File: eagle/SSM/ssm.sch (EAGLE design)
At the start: 21 parts, among them IC1 4051N, IC2 MCP604P

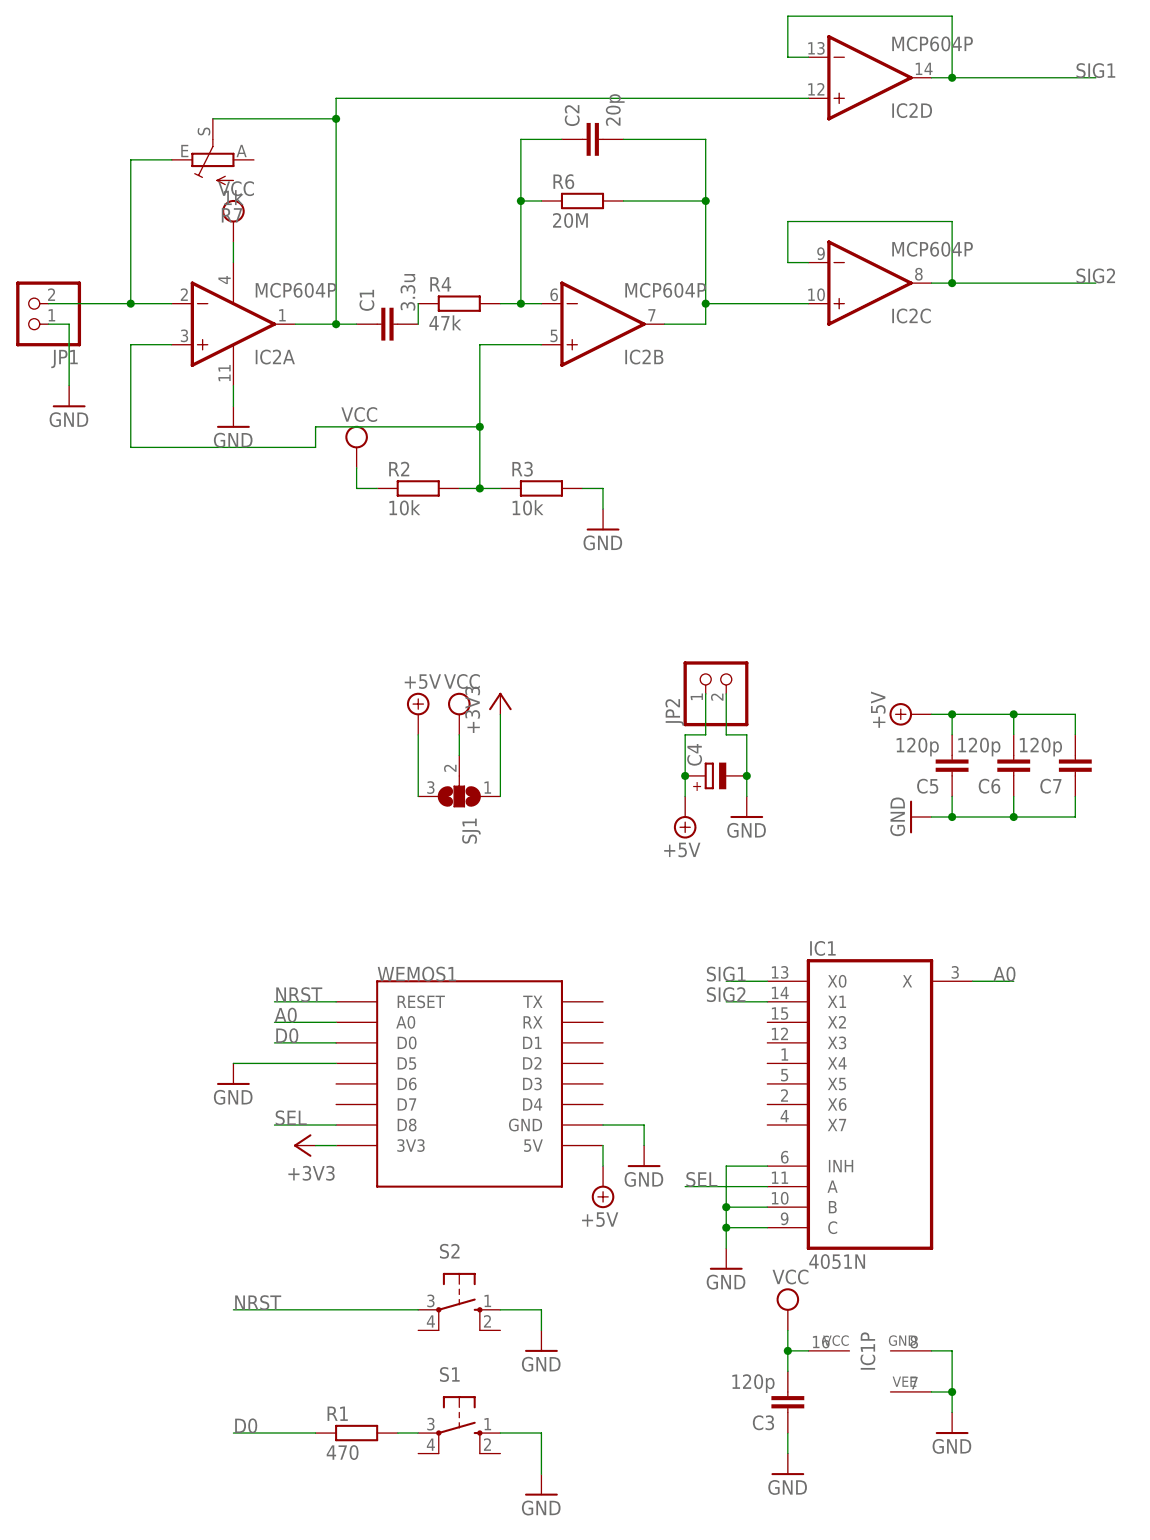
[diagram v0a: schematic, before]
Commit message: realign board for ordered parts
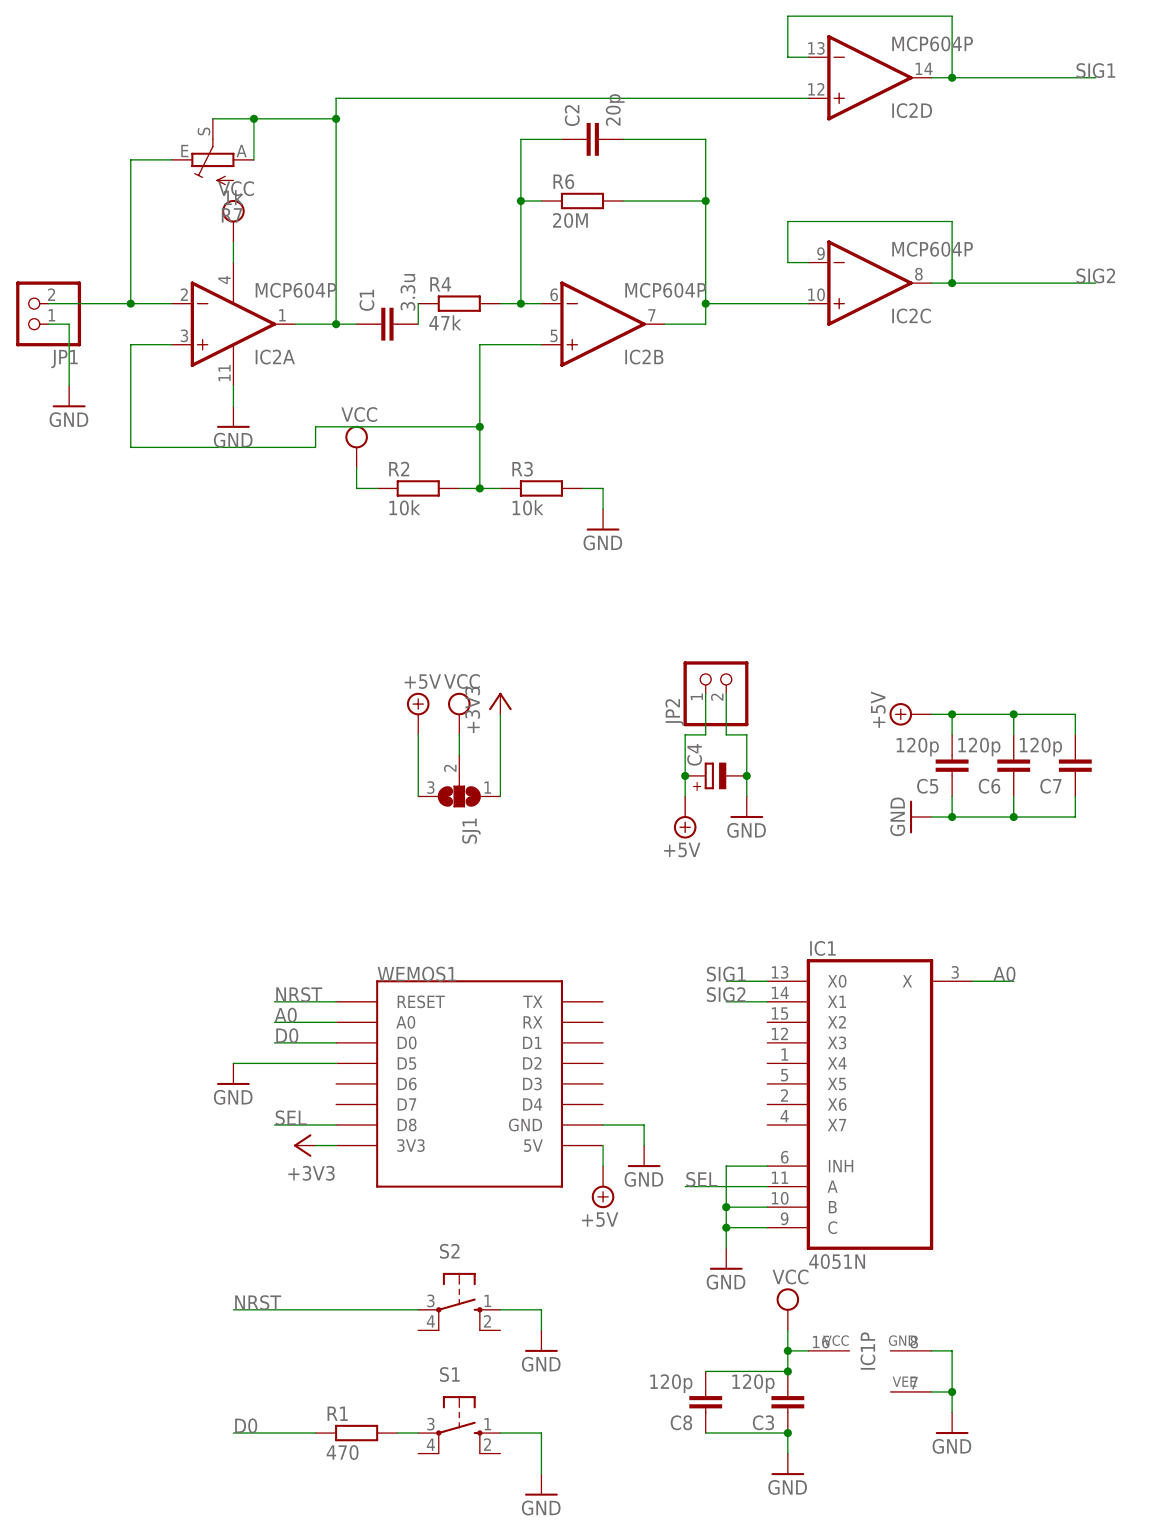
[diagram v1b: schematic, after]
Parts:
- added C8: 120p, rcl:C-EU025-024X044
- C1: device capacitor-wima:C5/3 -> Cap:C-EU
- C2, C3, C5, C6, C7: device capacitor-wima:C5/3 -> rcl:C-EU025-024X044
- R6: device resistor:R-EU_0204/7 -> rcl:R-EU_0207/10
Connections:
- net GND: now also C8.1
- net N$5: now also R7.A
- net VCC: now also C8.2
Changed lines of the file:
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@@
 <part name="GND4" library="supply1" library_urn="urn:adsk.eagle:library:371" deviceset="GND" device=""/>
 <part name="IC2" library="linear" deviceset="MCP604" device="P" value="MCP604P"/>
-<part name="P+1" library="supply2" deviceset="VCC" device=""/>
-<part name="P+2" library="supply2" deviceset="VCC" device=""/>
+<part name="P+1" library="supply2" library_urn="urn:adsk.eagle:library:372" deviceset="VCC" device=""/>
+<part name="P+2" library="supply2" library_urn="urn:adsk.eagle:library:372" deviceset="VCC" device=""/>
 <part name="R2" library="resistor" library_urn="urn:adsk.eagle:library:348" deviceset="R-EU_" device="0204/7" package3d_urn="urn:adsk.eagle:package:25945/1" value="10k"/>
 <part name="R3" library="resistor" library_urn="urn:adsk.eagle:library:348" deviceset="R-EU_" device="0204/7" package3d_urn="urn:adsk.eagle:package:25945/1" value="10k"/>
@@
 <part name="GND6" library="supply1" library_urn="urn:adsk.eagle:library:371" deviceset="GND" device=""/>
 <part name="R4" library="resistor" library_urn="urn:adsk.eagle:library:348" deviceset="R-EU_" device="0204/7" package3d_urn="urn:adsk.eagle:package:25945/1" value="47k"/>
-<part name="C1" library="capacitor-wima" library_urn="urn:adsk.eagle:library:116" deviceset="C" device="5/3" package3d_urn="urn:adsk.eagle:package:5433/1" value="3.3u"/>
-<part name="R6" library="resistor" library_urn="urn:adsk.eagle:library:348" deviceset="R-EU_" device="0204/7" package3d_urn="urn:adsk.eagle:package:25945/1" value="20M"/>
-<part name="C2" library="capacitor-wima" library_urn="urn:adsk.eagle:library:116" deviceset="C" device="5/3" package3d_urn="urn:adsk.eagle:package:5433/1" value="20p"/>
+<part name="C1" library="Cap" deviceset="C-EU" device="" value="3.3u"/>
+<part name="R6" library="rcl" library_urn="urn:adsk.eagle:library:334" deviceset="R-EU_" device="0207/10" package3d_urn="urn:adsk.eagle:package:23491/1" value="20M"/>
+<part name="C2" library="rcl" library_urn="urn:adsk.eagle:library:334" deviceset="C-EU" device="025-024X044" package3d_urn="urn:adsk.eagle:package:23630/1" value="20p"/>
 <part name="JP1" library="pinhead" library_urn="urn:adsk.eagle:library:325" deviceset="PINHD-1X2" device="" package3d_urn="urn:adsk.eagle:package:22435/2"/>
 <part name="GND7" library="supply1" library_urn="urn:adsk.eagle:library:371" deviceset="GND" device=""/>
 <part name="GND8" library="supply1" library_urn="urn:adsk.eagle:library:371" deviceset="GND" device=""/>
-<part name="P+3" library="supply2" deviceset="VCC" device=""/>
-<part name="R7" library="pot" deviceset="TRIM_EU-" device="B64Y" value="1k"/>
-<part name="P+4" library="supply2" deviceset="VCC" device=""/>
-<part name="SUPPLY1" library="supply2" deviceset="+5V" device=""/>
+<part name="P+3" library="supply2" library_urn="urn:adsk.eagle:library:372" deviceset="VCC" device=""/>
+<part name="R7" library="pot" library_urn="urn:adsk.eagle:library:331" deviceset="TRIM_EU-" device="B64Y" package3d_urn="urn:adsk.eagle:package:22690/1" value="1k"/>
+<part name="P+4" library="supply2" library_urn="urn:adsk.eagle:library:372" deviceset="VCC" device=""/>
+<part name="SUPPLY1" library="supply2" library_urn="urn:adsk.eagle:library:372" deviceset="+5V" device=""/>
 <part name="+3V1" library="supply1" deviceset="+3V3" device=""/>
 <part name="+3V2" library="supply1" deviceset="+3V3" device=""/>
-<part name="SUPPLY2" library="supply2" deviceset="+5V" device=""/>
-<part name="SJ1" library="jumper" deviceset="SJ2W" device=""/>
+<part name="SUPPLY2" library="supply2" library_urn="urn:adsk.eagle:library:372" deviceset="+5V" device=""/>
+<part name="SJ1" library="jumper" library_urn="urn:adsk.eagle:library:252" deviceset="SJ2W" device="" package3d_urn="urn:adsk.eagle:package:15474/1"/>
 <part name="GND9" library="supply1" library_urn="urn:adsk.eagle:library:371" deviceset="GND" device=""/>
 <part name="JP2" library="pinhead" library_urn="urn:adsk.eagle:library:325" deviceset="PINHD-1X2" device="" package3d_urn="urn:adsk.eagle:package:22435/2"/>
-<part name="SUPPLY3" library="supply2" deviceset="+5V" device=""/>
+<part name="SUPPLY3" library="supply2" library_urn="urn:adsk.eagle:library:372" deviceset="+5V" device=""/>
 <part name="GND10" library="supply1" library_urn="urn:adsk.eagle:library:371" deviceset="GND" device=""/>
-<part name="C3" library="capacitor-wima" library_urn="urn:adsk.eagle:library:116" deviceset="C" device="5/3" package3d_urn="urn:adsk.eagle:package:5433/1" value="120p"/>
+<part name="C3" library="rcl" library_urn="urn:adsk.eagle:library:334" deviceset="C-EU" device="025-024X044" package3d_urn="urn:adsk.eagle:package:23630/1" value="120p"/>
 <part name="GND11" library="supply1" library_urn="urn:adsk.eagle:library:371" deviceset="GND" device=""/>
-<part name="C4" library="rcl" deviceset="CPOL-EU" device="E2.5-5"/>
-<part name="SUPPLY4" library="supply2" deviceset="+5V" device=""/>
+<part name="C4" library="rcl" library_urn="urn:adsk.eagle:library:334" deviceset="CPOL-EU" device="E2.5-5" package3d_urn="urn:adsk.eagle:package:23344/1"/>
+<part name="SUPPLY4" library="supply2" library_urn="urn:adsk.eagle:library:372" deviceset="+5V" device=""/>
 <part name="GND12" library="supply1" library_urn="urn:adsk.eagle:library:371" deviceset="GND" device=""/>
-<part name="C5" library="capacitor-wima" library_urn="urn:adsk.eagle:library:116" deviceset="C" device="5/3" package3d_urn="urn:adsk.eagle:package:5433/1" value="120p"/>
-<part name="C6" library="capacitor-wima" library_urn="urn:adsk.eagle:library:116" deviceset="C" device="5/3" package3d_urn="urn:adsk.eagle:package:5433/1" value="120p"/>
-<part name="C7" library="capacitor-wima" library_urn="urn:adsk.eagle:library:116" deviceset="C" device="5/3" package3d_urn="urn:adsk.eagle:package:5433/1" value="120p"/>
+<part name="C5" library="rcl" library_urn="urn:adsk.eagle:library:334" deviceset="C-EU" device="025-024X044" package3d_urn="urn:adsk.eagle:package:23630/1" value="120p"/>
+<part name="C6" library="rcl" library_urn="urn:adsk.eagle:library:334" deviceset="C-EU" device="025-024X044" package3d_urn="urn:adsk.eagle:package:23630/1" value="120p"/>
+<part name="C7" library="rcl" library_urn="urn:adsk.eagle:library:334" deviceset="C-EU" device="025-024X044" package3d_urn="urn:adsk.eagle:package:23630/1" value="120p"/>
+<part name="C8" library="rcl" library_urn="urn:adsk.eagle:library:334" deviceset="C-EU" device="025-024X044" package3d_urn="urn:adsk.eagle:package:23630/1" value="120p"/>
 </parts>
 <sheets>
@@
 <instance part="C6" gate="G$1" x="109.22" y="109.22" rot="R180"/>
 <instance part="C7" gate="G$1" x="116.84" y="109.22" rot="R180"/>
+<instance part="C8" gate="G$1" x="71.12" y="30.48" rot="R180"/>
 </instances>
 <busses>
@@
 <pinref part="GND11" gate="1" pin="GND"/>
 <wire x1="81.28" y1="27.94" x2="81.28" y2="25.4" width="0.1524" layer="91"/>
+<pinref part="C8" gate="G$1" pin="1"/>
+<wire x1="81.28" y1="27.94" x2="71.12" y2="27.94" width="0.1524" layer="91"/>
+<junction x="81.28" y="27.94"/>
 </segment>
 <segment>
@@
 <wire x1="83.82" y1="193.04" x2="25.4" y2="193.04" width="0.1524" layer="91"/>
 <pinref part="R7" gate="1" pin="S"/>
-<wire x1="10.16" y1="190.5" x2="25.4" y2="190.5" width="0.1524" layer="91"/>
+<wire x1="10.16" y1="190.5" x2="15.24" y2="190.5" width="0.1524" layer="91"/>
 <junction x="25.4" y="190.5"/>
+<pinref part="R7" gate="1" pin="A"/>
+<wire x1="15.24" y1="190.5" x2="25.4" y2="190.5" width="0.1524" layer="91"/>
+<wire x1="15.24" y1="185.42" x2="15.24" y2="190.5" width="0.1524" layer="91"/>
+<junction x="15.24" y="190.5"/>
 </segment>
 </net>
@@
 <wire x1="81.28" y1="38.1" x2="81.28" y2="35.56" width="0.1524" layer="91"/>
 <junction x="81.28" y="38.1"/>
-</segment>
-<segment>
+<pinref part="C8" gate="G$1" pin="2"/>
+<wire x1="71.12" y1="35.56" x2="81.28" y2="35.56" width="0.1524" layer="91"/>
+<junction x="81.28" y="35.56"/>
+</segment>
+<segment>
